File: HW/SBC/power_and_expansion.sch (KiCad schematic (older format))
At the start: 11 parts, among them J4 BARREL_JACK, J8 JTAG, U12 LM7805CT

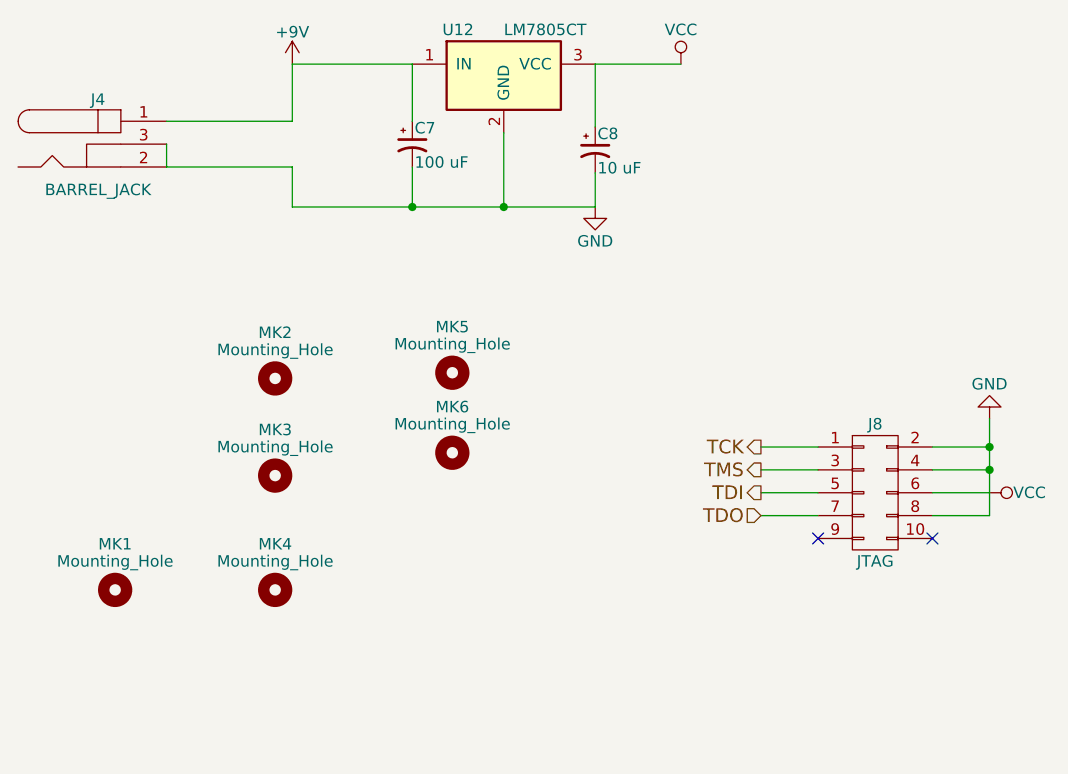
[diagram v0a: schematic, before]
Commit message: Added CPLD to schematics. Updates rest of schematics to use CPLD
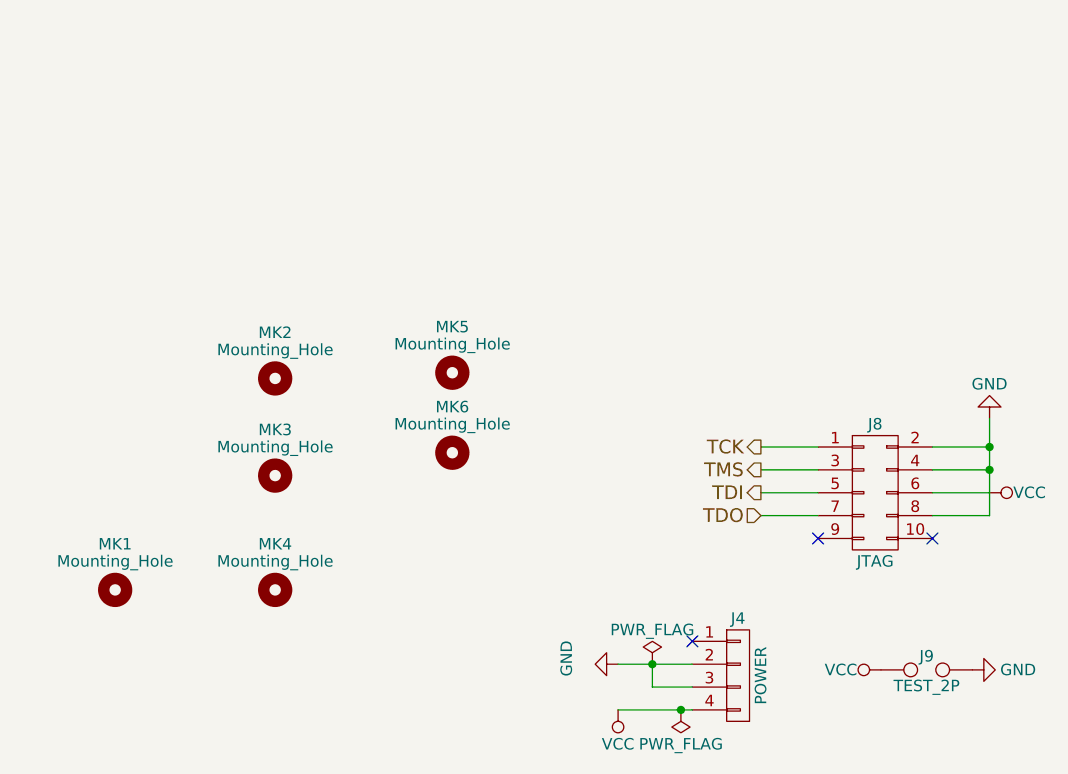
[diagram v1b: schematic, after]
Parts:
- removed C7: 100 uF, Capacitors_ThroughHole:CP_Radial_D6.3mm_P2.50mm, symbol CP1_Small
- removed C8: 10 uF, Capacitors_ThroughHole:CP_Radial_D5.0mm_P2.00mm, symbol CP1_Small
- removed J4: BARREL_JACK, Connect:BARREL_JACK, symbol BARREL_JACK
- removed U12: LM7805CT, TO_SOT_Packages_THT:TO-220-3_Horizontal, symbol LM7805CT-RESCUE-pluto
- added J4: POWER, Connectors_Molex:Molex_NanoFit_1x04x2.50mm_Angled, symbol CONN_01X04
- added J9: TEST_2P, Pin_Headers:Pin_Header_Straight_1x02_Pitch2.54mm, symbol TEST_2P
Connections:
- net GND: now also J4.2 (P2), J4.3 (P3), J9.2
- net VCC: now also J4.4 (P4), J9.1
- no-connect marks 2 -> 3
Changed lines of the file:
@@
 $Descr A4 11693 8268
 encoding utf-8
-Sheet 5 8
+Sheet 5 7
 Title "Power supply and mounting holes"
 Date "2017-06-07"
@@
 $EndComp
 $Comp
-L GND #PWR033
-U 1 1 5938552A
-P 3225 2275
-F 0 "#PWR033" H 3225 2025 50  0001 C CNN
-F 1 "GND" H 3225 2125 50  0000 C CNN
-F 2 "" H 3225 2275 50  0001 C CNN
-F 3 "" H 3225 2275 50  0001 C CNN
-	1    3225 2275
-	1    0    0    -1
-$EndComp
-$Comp
-L BARREL_JACK J4
-U 1 1 5930508B
-P 1050 2000
-F 0 "J4" H 1050 2195 50  0000 C CNN
-F 1 "BARREL_JACK" H 1050 1800 50  0000 C CNN
-F 2 "Connect:BARREL_JACK" H 1050 2000 50  0001 C CNN
-F 3 "" H 1050 2000 50  0001 C CNN
-	1    1050 2000
-	1    0    0    -1
-$EndComp
-$Comp
-L VCC #PWR034
-U 1 1 58D5EE10
-P 3600 1650
-F 0 "#PWR034" H 3600 1500 50  0001 C CNN
-F 1 "VCC" H 3600 1800 50  0000 C CNN
-F 2 "" H 3600 1650 50  0001 C CNN
-F 3 "" H 3600 1650 50  0001 C CNN
-	1    3600 1650
-	1    0    0    -1
-$EndComp
-$Comp
-L CP1_Small C7
-U 1 1 58D5E9AB
-P 2425 2000
-F 0 "C7" H 2435 2070 50  0000 L CNN
-F 1 "100 uF" H 2435 1920 50  0000 L CNN
-F 2 "Capacitors_ThroughHole:CP_Radial_D6.3mm_P2.50mm" H 2425 2000 50  0001 C CNN
-F 3 "" H 2425 2000 50  0001 C CNN
-	1    2425 2000
-	1    0    0    -1
-$EndComp
-$Comp
-L CP1_Small C8
-U 1 1 58D5EA6C
-P 3225 2025
-F 0 "C8" H 3235 2095 50  0000 L CNN
-F 1 "10 uF" H 3235 1945 50  0000 L CNN
-F 2 "Capacitors_ThroughHole:CP_Radial_D5.0mm_P2.00mm" H 3225 2025 50  0001 C CNN
-F 3 "" H 3225 2025 50  0001 C CNN
-	1    3225 2025
-	1    0    0    -1
-$EndComp
-$Comp
-L LM7805CT-RESCUE-pluto U12
-U 1 1 58E10ED4
-P 2825 1700
-F 0 "U12" H 2625 1900 50  0000 C CNN
-F 1 "LM7805CT" H 2825 1900 50  0000 L CNN
-F 2 "TO_SOT_Packages_THT:TO-220-3_Horizontal" H 2825 1800 50  0001 C CIN
-F 3 "" H 2825 1700 50  0001 C CNN
-	1    2825 1700
-	1    0    0    -1
-$EndComp
-$Comp
-L +9V #PWR035
-U 1 1 593AD94D
-P 1900 1650
-F 0 "#PWR035" H 1900 1500 50  0001 C CNN
-F 1 "+9V" H 1900 1790 50  0000 C CNN
-F 2 "" H 1900 1650 50  0001 C CNN
-F 3 "" H 1900 1650 50  0001 C CNN
-	1    1900 1650
-	1    0    0    -1
-$EndComp
-$Comp
 L CONN_02X05 J8
 U 1 1 59F22BEE
@@
 TMS
 Wire Wire Line
-	1900 2275 3225 2275
-Wire Wire Line
-	2425 1650 1900 1650
-Wire Wire Line
-	1350 1900 1900 1900
-Wire Wire Line
-	1900 1900 1900 1650
-Wire Wire Line
-	1350 2100 1900 2100
-Wire Wire Line
-	1900 2100 1900 2275
-Wire Wire Line
-	3225 1650 3600 1650
-Wire Wire Line
-	2825 2275 2825 1950
-Connection ~ 2825 2275
-Connection ~ 2425 2275
-Wire Wire Line
-	3225 2275 3225 2125
-Wire Wire Line
-	3225 1650 3225 1925
-Wire Wire Line
-	2425 1900 2425 1650
-Wire Wire Line
-	2425 2100 2425 2275
-Wire Wire Line
-	1350 2000 1350 2100
-Wire Wire Line
 	3950 3325 4200 3325
 Wire Wire Line
@@
 Connection ~ 4950 3325
 $Comp
-L GND #PWR036
+L GND #PWR035
 U 1 1 59F407A0
 P 4950 3200
-F 0 "#PWR036" H 4950 2950 50  0001 C CNN
+F 0 "#PWR035" H 4950 2950 50  0001 C CNN
 F 1 "GND" H 4950 3050 50  0000 C CNN
 F 2 "" H 4950 3200 50  0001 C CNN
@@
 $EndComp
 $Comp
-L VCC #PWR037
+L VCC #PWR036
 U 1 1 59F407C6
 P 4950 3525
-F 0 "#PWR037" H 4950 3375 50  0001 C CNN
+F 0 "#PWR036" H 4950 3375 50  0001 C CNN
 F 1 "VCC" V 4950 3700 50  0000 C CNN
 F 2 "" H 4950 3525 50  0001 C CNN
@@
 	1    0    0    -1
 $EndComp
+$Comp
+L CONN_01X04 J4
+U 1 1 5A1609CD
+P 3850 4325
+F 0 "J4" H 3850 4575 50  0000 C CNN
+F 1 "POWER" V 3950 4325 50  0000 C CNN
+F 2 "Connectors_Molex:Molex_NanoFit_1x04x2.50mm_Angled" H 3850 4325 50  0001 C CNN
+F 3 "" H 3850 4325 50  0001 C CNN
+	1    3850 4325
+	1    0    0    -1
+$EndComp
+Wire Wire Line
+	3325 4275 3650 4275
+Wire Wire Line
+	3475 4375 3650 4375
+$Comp
+L VCC #PWR037
+U 1 1 5A160A6E
+P 3325 4475
+F 0 "#PWR037" H 3325 4325 50  0001 C CNN
+F 1 "VCC" H 3325 4625 50  0000 C CNN
+F 2 "" H 3325 4475 50  0001 C CNN
+F 3 "" H 3325 4475 50  0001 C CNN
+	1    3325 4475
+	-1   0    0    1
+$EndComp
+$Comp
+L GND #PWR038
+U 1 1 5A160AE2
+P 3325 4275
+F 0 "#PWR038" H 3325 4025 50  0001 C CNN
+F 1 "GND" H 3300 4050 50  0000 C CNN
+F 2 "" H 3325 4275 50  0001 C CNN
+F 3 "" H 3325 4275 50  0001 C CNN
+	1    3325 4275
+	0    1    1    0
+$EndComp
+Wire Wire Line
+	3325 4475 3650 4475
+NoConn ~ 3650 4175
+$Comp
+L TEST_2P J9
+U 1 1 5A164D68
+P 4675 4300
+F 0 "J9" H 4675 4360 50  0000 C CNN
+F 1 "TEST_2P" H 4675 4230 50  0000 C CNN
+F 2 "Pin_Headers:Pin_Header_Straight_1x02_Pitch2.54mm" H 4675 4300 50  0001 C CNN
+F 3 "" H 4675 4300 50  0001 C CNN
+	1    4675 4300
+	1    0    0    -1
+$EndComp
+$Comp
+L GND #PWR039
+U 1 1 5A164DA9
+P 4875 4300
+F 0 "#PWR039" H 4875 4050 50  0001 C CNN
+F 1 "GND" V 4875 4100 50  0000 C CNN
+F 2 "" H 4875 4300 50  0001 C CNN
+F 3 "" H 4875 4300 50  0001 C CNN
+	1    4875 4300
+	0    -1   -1   0
+$EndComp
+$Comp
+L VCC #PWR040
+U 1 1 5A164DEA
+P 4475 4300
+F 0 "#PWR040" H 4475 4150 50  0001 C CNN
+F 1 "VCC" V 4475 4475 50  0000 C CNN
+F 2 "" H 4475 4300 50  0001 C CNN
+F 3 "" H 4475 4300 50  0001 C CNN
+	1    4475 4300
+	0    -1   -1   0
+$EndComp
+$Comp
+L PWR_FLAG #FLG041
+U 1 1 5A171315
+P 3475 4275
+F 0 "#FLG041" H 3475 4350 50  0001 C CNN
+F 1 "PWR_FLAG" H 3475 4425 50  0000 C CNN
+F 2 "" H 3475 4275 50  0001 C CNN
+F 3 "" H 3475 4275 50  0001 C CNN
+	1    3475 4275
+	1    0    0    -1
+$EndComp
+Connection ~ 3475 4275
+$Comp
+L PWR_FLAG #FLG042
+U 1 1 5A171393
+P 3600 4475
+F 0 "#FLG042" H 3600 4550 50  0001 C CNN
+F 1 "PWR_FLAG" H 3600 4625 50  0000 C CNN
+F 2 "" H 3600 4475 50  0001 C CNN
+F 3 "" H 3600 4475 50  0001 C CNN
+	1    3600 4475
+	-1   0    0    1
+$EndComp
+Connection ~ 3600 4475
+Wire Wire Line
+	3475 4275 3475 4375
 $EndSCHEMATC
